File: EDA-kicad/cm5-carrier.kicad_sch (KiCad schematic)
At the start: 6 parts

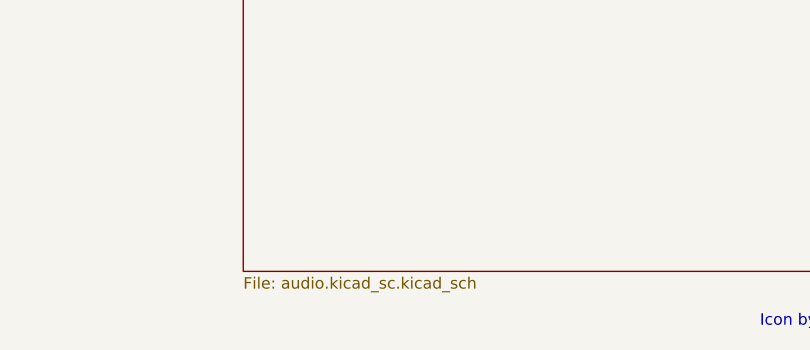
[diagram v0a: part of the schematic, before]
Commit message: Fixed audio schematic file name
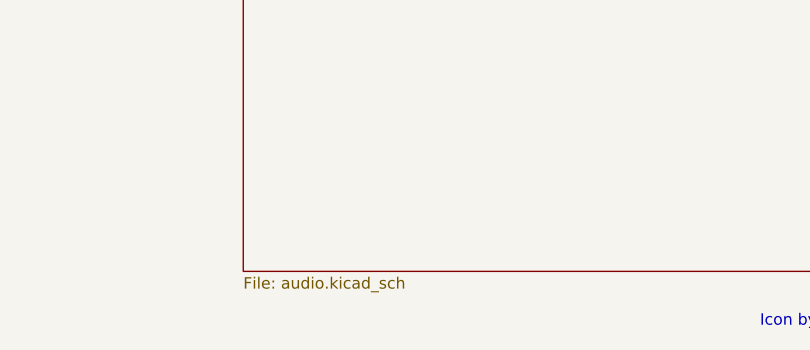
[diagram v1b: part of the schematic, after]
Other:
- sheet Audio: file audio.kicad_sc.kicad_sch -> audio.kicad_sch
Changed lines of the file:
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@@
 			)
 		)
-		(property "Sheetfile" "audio.kicad_sc.kicad_sch"
+		(property "Sheetfile" "audio.kicad_sch"
 			(at 293.37 424.2566 0)
 			(effects

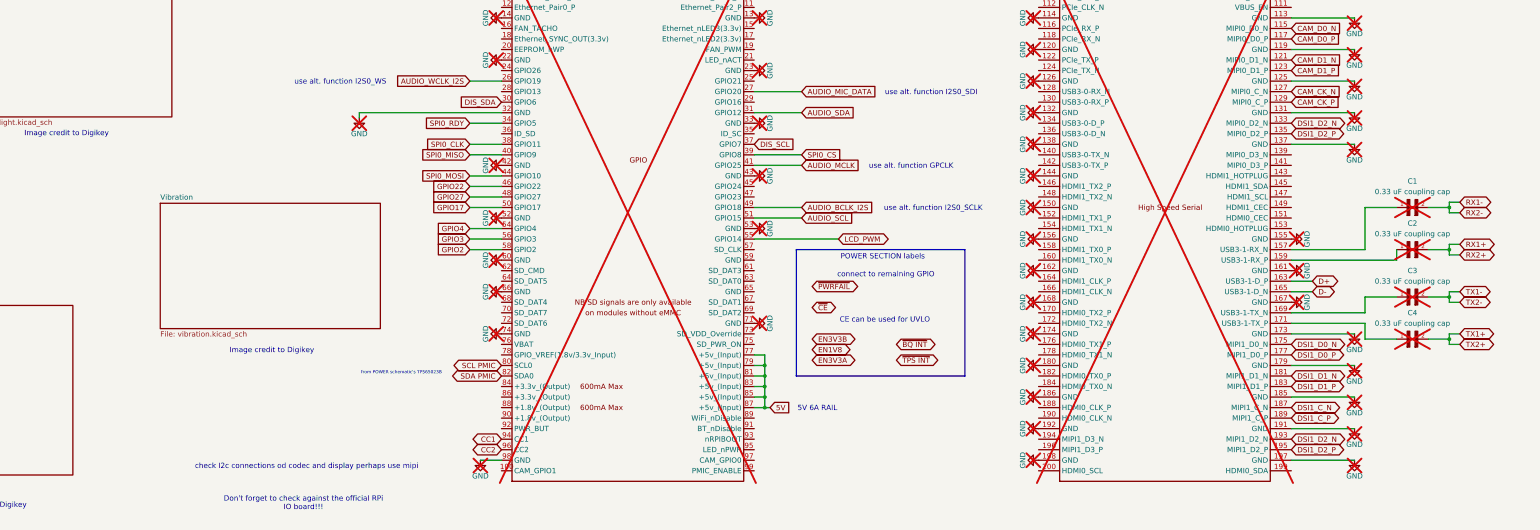
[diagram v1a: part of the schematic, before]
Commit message: Finished audio schematic
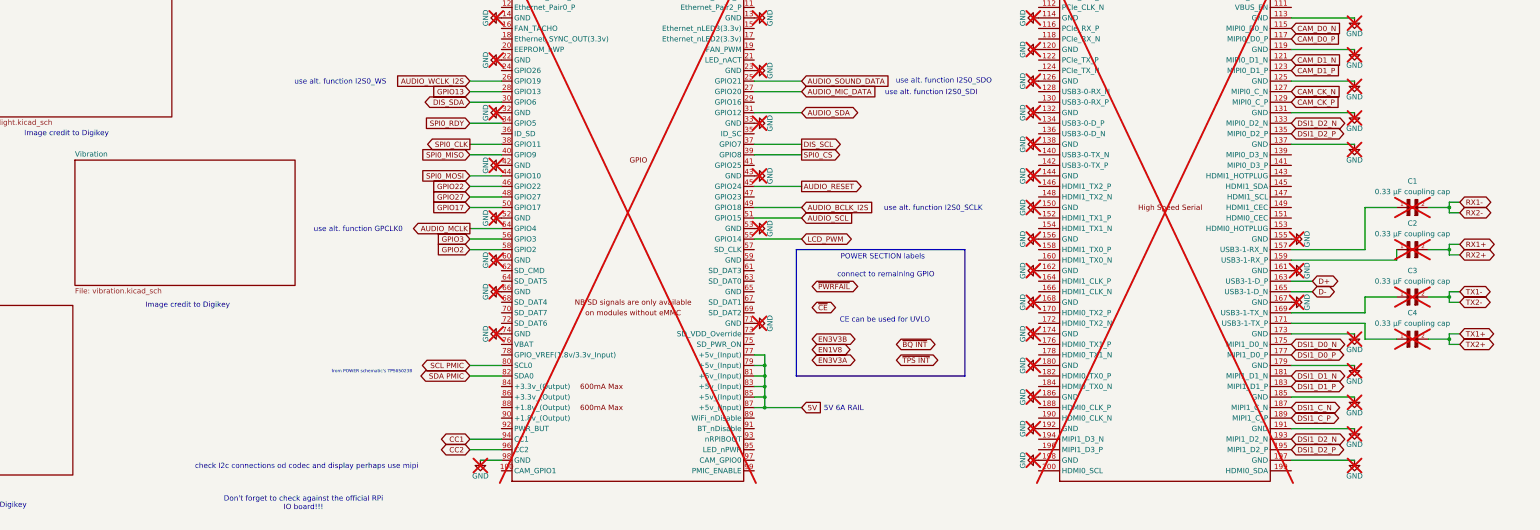
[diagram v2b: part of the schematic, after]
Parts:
- C1, C2, C3, C4: value 0.33 uF coupling cap -> 0.33 µF coupling cap
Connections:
- net GPIO4 is gone; now on net AUDIO_MCLK: Module1.54 (GPIO4)
- net AUDIO_MCLK: no longer Module1.41 (GPIO25)
- net AUDIO_SOUND_DATA: now reaches Module1.25 (GPIO21)
- net GPIO13: now reaches Module1.28 (GPIO13)
- net AUDIO_RESET: now reaches Module1.45 (GPIO24)
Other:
- note added: "use alt. function GPCLK0"
- note added: "use alt. function I2S0_SDO"
- note removed: "use alt. function GPCLK"

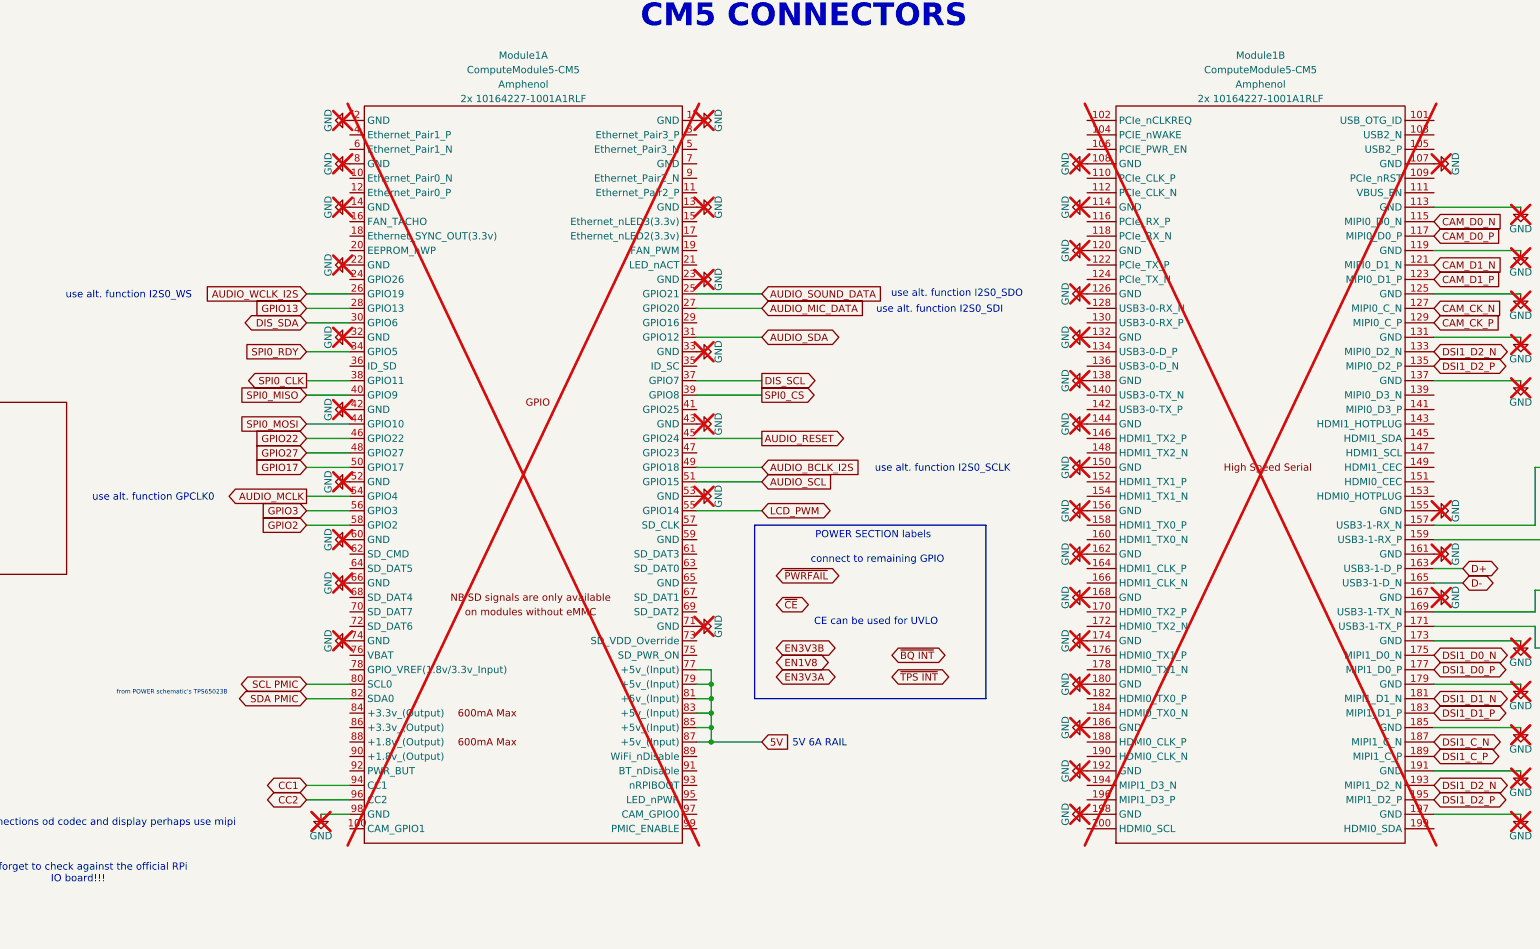
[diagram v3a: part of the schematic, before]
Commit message: charger 50% routed
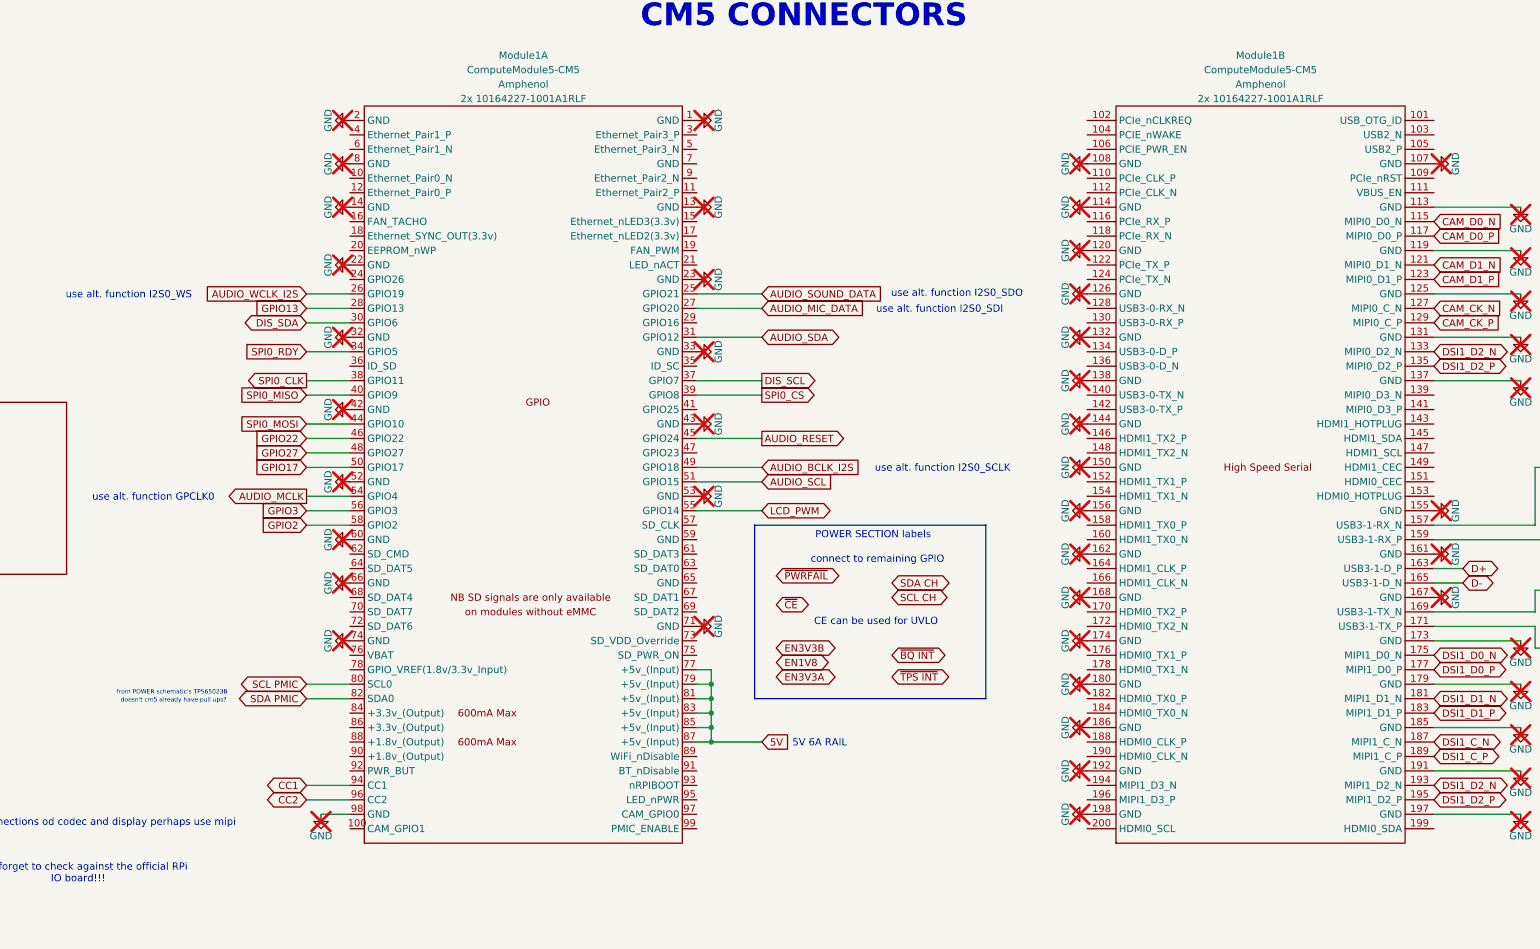
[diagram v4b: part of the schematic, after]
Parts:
- Module1: now fitted
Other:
- note added: "doesn't cm5 already have pull ups?"
